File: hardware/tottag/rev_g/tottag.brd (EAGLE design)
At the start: 68.1 x 39.5 mm, 198 parts, among them J1 USB4110-GF-A, J2 DM3AT-SF-PEJM5, J3 TC2030-JLINK-NL-2SIDE, J4 TC2030-JLINK-NL-2SIDE, J5 MOLEX-PICO-SPOX-3SIDE, Q1 CSD75207W15, Q4 CSD75207W15, T1 HHM1595A1, U1 DW1000, U10 STM32F091CC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

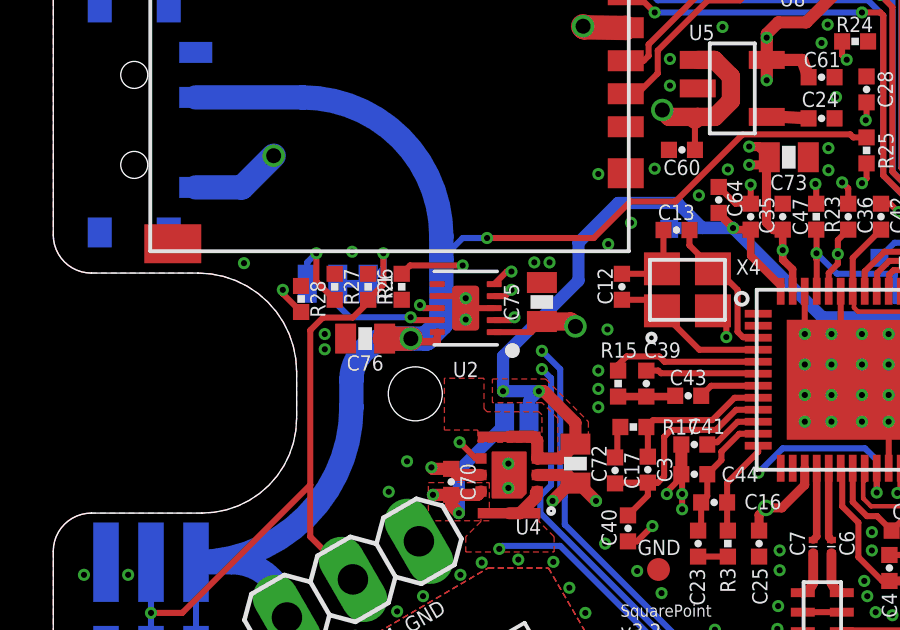
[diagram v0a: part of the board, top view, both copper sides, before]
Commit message: rev_g: design review fixes
 - Unify `!AD_EN` naming
 - C75/C76 10µF -> 1µF
 - Add battery pack details
 - Add NTC math details
 - Clarify switch on power diagram
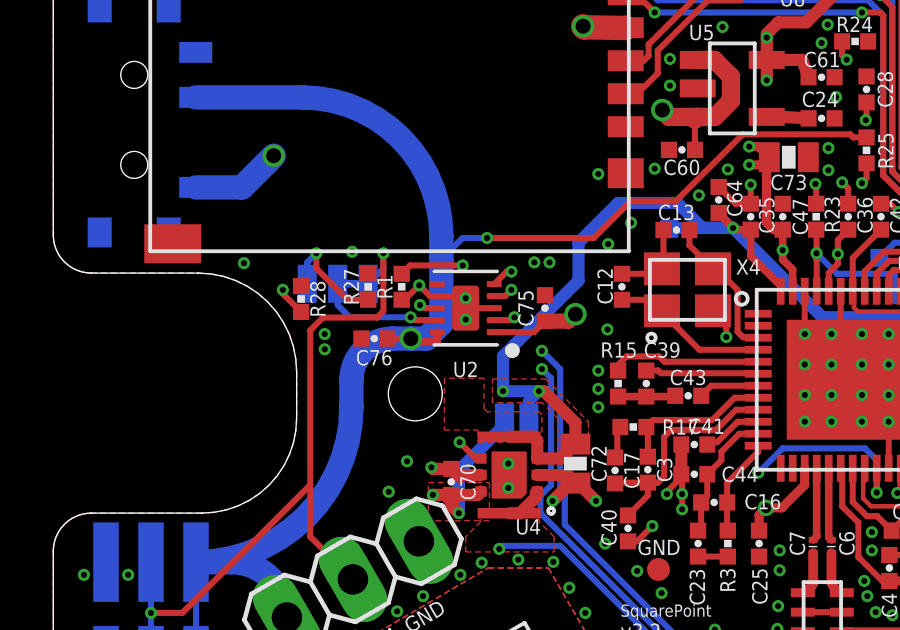
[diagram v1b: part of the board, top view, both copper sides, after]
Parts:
- removed R26: 249k, passives:0402_RES
- C75, C76: value 10uF -> 1uF; device passives:0603_CAP -> passives:0402_CAP
- moved R27 1.12 mm to (-23.6, 17.1)
- moved C76 0.30 mm to (-23.4, 15.3)
- moved C75 0.23 mm to (-17.7, 16.4)
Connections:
- net !AD-EN renamed !AD_EN
- net BATT_THERM: no longer R26.2
- net GND: no longer R26.1
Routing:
- net GND: track 148.3 -> 149.8 mm, vias 516 -> 517
- net N$47: track 2.95 -> 3.81 mm

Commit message: rev_g: correct thermistor prefix (R36 -> RT1)
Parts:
- renumbered R36 to RT1
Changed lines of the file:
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@@
 <attribute name="VALUE" x="1.7526" y="-4.3942" size="0.508" layer="27" font="vector" ratio="18" rot="R180" align="bottom-center"/>
 </element>
-<element name="R36" library="passives" library_urn="urn:adsk.eagle:library:20904581" package="0402_RES" package3d_urn="urn:adsk.eagle:package:20904668/2" value="10k@25C" x="0.9144" y="-3.0734" smashed="yes" rot="R270">
+<element name="RT1" library="passives" library_urn="urn:adsk.eagle:library:20904581" package="0402_RES" package3d_urn="urn:adsk.eagle:package:20904668/2" value="10k@25C" x="0.9144" y="-3.0734" smashed="yes" rot="R270">
 <attribute name="NAME" x="1.2954" y="-3.0734" size="0.508" layer="25" font="vector" ratio="18" rot="R270" align="bottom-center"/>
 <attribute name="VALUE" x="-0.4826" y="-3.0734" size="0.508" layer="27" font="vector" ratio="18" rot="R270" align="bottom-center"/>
@@
 <signal name="N$68">
 <contactref element="JP3" pad="3"/>
-<contactref element="R36" pad="2"/>
+<contactref element="RT1" pad="2"/>
 <wire x1="1.4224" y1="-3.4544" x2="1.4224" y2="-3.2512" width="0.2032" layer="16"/>
 <wire x1="1.4224" y1="-3.2512" x2="1.9304" y2="-2.7432" width="0.2032" layer="16"/>
@@
 </signal>
 <signal name="N$69">
-<contactref element="R36" pad="1"/>
+<contactref element="RT1" pad="1"/>
 <contactref element="R37" pad="2"/>
 <wire x1="0.9144" y1="-2.64033125" x2="0.9144" y2="-1.65226875" width="0.2032" layer="1"/>

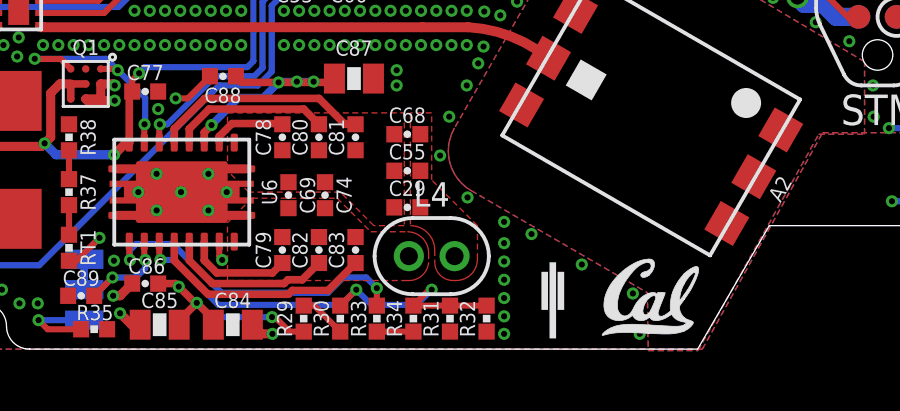
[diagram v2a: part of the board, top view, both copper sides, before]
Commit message: rev_g: Fix R31, R32 series / parallel
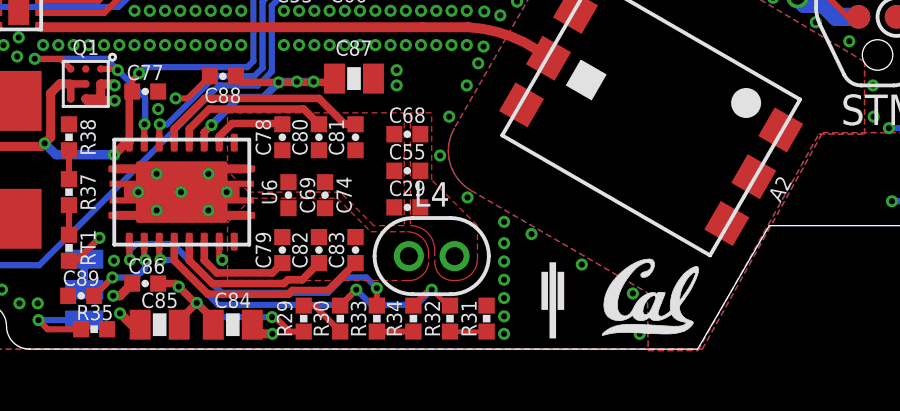
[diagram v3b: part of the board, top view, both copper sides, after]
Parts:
- moved R31 1.22 mm to (14.8, -5.44)
- moved R32 1.22 mm to (13.6, -5.44), turned to 270 degrees
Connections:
- new net N$28: R31.1, R32.2
- net BQ_FOD: now also R32.1; no longer R31.2, R32.2
- net GND: now also R31.2; no longer R31.1, R32.1
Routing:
- net BQ_FOD: track 14.9 -> 13.3 mm
- net N$28: track 0.00 -> 1.22 mm
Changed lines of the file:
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@@
 <attribute name="VALUE" x="11.3538" y="-5.4356" size="0.508" layer="27" font="vector" ratio="18" rot="R90" align="bottom-center"/>
 </element>
-<element name="R31" library="passives" library_urn="urn:adsk.eagle:library:20904581" package="0402_RES" package3d_urn="urn:adsk.eagle:package:20904668/2" value="97.6" x="13.6144" y="-5.4356" smashed="yes" rot="R90">
-<attribute name="DIGIKEY" value="RMCF0402FT97R6CT-ND" x="13.6144" y="-5.4356" size="1.778" layer="27" rot="R90" display="off"/>
-<attribute name="MPN" value="RMCF0402FT97R6" x="13.6144" y="-5.4356" size="1.778" layer="27" rot="R90" display="off"/>
-<attribute name="NAME" x="13.2334" y="-5.4356" size="0.508" layer="25" font="vector" ratio="18" rot="R90" align="bottom-center"/>
-<attribute name="VALUE" x="15.0114" y="-5.4356" size="0.508" layer="27" font="vector" ratio="18" rot="R90" align="bottom-center"/>
-</element>
-<element name="R32" library="passives" library_urn="urn:adsk.eagle:library:20904581" package="0402_RES" package3d_urn="urn:adsk.eagle:package:20904668/2" value="97.6" x="14.8336" y="-5.4356" smashed="yes" rot="R90">
+<element name="R31" library="passives" library_urn="urn:adsk.eagle:library:20904581" package="0402_RES" package3d_urn="urn:adsk.eagle:package:20904668/2" value="97.6" x="14.8336" y="-5.4356" smashed="yes" rot="R90">
 <attribute name="DIGIKEY" value="RMCF0402FT97R6CT-ND" x="14.8336" y="-5.4356" size="1.778" layer="27" rot="R90" display="off"/>
 <attribute name="MPN" value="RMCF0402FT97R6" x="14.8336" y="-5.4356" size="1.778" layer="27" rot="R90" display="off"/>
-<attribute name="NAME" x="14.4526" y="-5.4356" size="0.508" layer="25" font="vector" ratio="18" rot="R90" align="bottom-center"/>
+<attribute name="NAME" x="14.5034" y="-5.4356" size="0.508" layer="25" font="vector" ratio="18" rot="R90" align="bottom-center"/>
 <attribute name="VALUE" x="16.2306" y="-5.4356" size="0.508" layer="27" font="vector" ratio="18" rot="R90" align="bottom-center"/>
 </element>
+<element name="R32" library="passives" library_urn="urn:adsk.eagle:library:20904581" package="0402_RES" package3d_urn="urn:adsk.eagle:package:20904668/2" value="97.6" x="13.6144" y="-5.4356" smashed="yes" rot="R270">
+<attribute name="DIGIKEY" value="RMCF0402FT97R6CT-ND" x="13.6144" y="-5.4356" size="1.778" layer="27" rot="R270" display="off"/>
+<attribute name="MPN" value="RMCF0402FT97R6" x="13.6144" y="-5.4356" size="1.778" layer="27" rot="R270" display="off"/>
+<attribute name="NAME" x="13.2842" y="-5.4356" size="0.508" layer="25" font="vector" ratio="18" rot="R90" align="bottom-center"/>
+<attribute name="VALUE" x="12.2174" y="-5.4356" size="0.508" layer="27" font="vector" ratio="18" rot="R270" align="bottom-center"/>
+</element>
 <element name="R33" library="passives" library_urn="urn:adsk.eagle:library:20904581" package="0402_RES" package3d_urn="urn:adsk.eagle:package:20904668/2" value="162" x="11.176" y="-5.4356" smashed="yes" rot="R270">
 <attribute name="DIGIKEY" value="RMCF0402FT162RCT-ND" x="11.176" y="-5.4356" size="1.778" layer="27" rot="R270" display="off"/>
@@
 <contactref element="U6" pad="1"/>
 <contactref element="U6" pad="PAD"/>
-<contactref element="R31" pad="1"/>
-<contactref element="R32" pad="1"/>
 <via x="19.7104" y="-4.5974" extent="1-16" drill="0.2032"/>
 <via x="18.0086" y="-3.6322" extent="1-16" drill="0.2032"/>
@@
 <wire x1="-21.27" y1="16.7576" x2="-21.5074" y2="16.7576" width="0.2032" layer="1"/>
 <wire x1="-21.5074" y1="16.7576" x2="-21.8694" y2="17.1196" width="0.2032" layer="1"/>
+<contactref element="R31" pad="2"/>
 </signal>
 <signal name="VUSB">
@@
 </signal>
 <signal name="BQ_FOD">
-<contactref element="R31" pad="2"/>
-<contactref element="R32" pad="2"/>
 <contactref element="U6" pad="14"/>
 <contactref element="R30" pad="2"/>
 <contactref element="R34" pad="2"/>
-<wire x1="14.8336" y1="-5.00253125" x2="13.6144" y2="-5.00253125" width="0.2032" layer="1"/>
-<wire x1="13.6144" y1="-5.00253125" x2="12.3952" y2="-5.00253125" width="0.2032" layer="1"/>
 <wire x1="3.9236" y1="-2.8692" x2="3.9236" y2="-3.441" width="0.2032" layer="1"/>
 <wire x1="3.9236" y1="-3.441" x2="3.9624" y2="-3.4798" width="0.2032" layer="1"/>
@@
 <wire x1="12.4968" y1="-4.9784" x2="13.0048" y2="-4.4704" width="0.2032" layer="16"/>
 <wire x1="10.9982" y1="-4.9784" x2="12.4968" y2="-4.9784" width="0.2032" layer="16"/>
+<contactref element="R32" pad="1"/>
+<wire x1="13.6144" y1="-5.00253125" x2="13.53693125" y2="-5.00253125" width="0.1524" layer="1"/>
+<wire x1="13.53693125" y1="-5.00253125" x2="13.0048" y2="-4.4704" width="0.1524" layer="1"/>
 </signal>
 <signal name="BQ_RECT">
@@
 <via x="-18.8976" y="10.3632" extent="1-16" drill="0.2032"/>
 </signal>
+<signal name="N$28">
+<contactref element="R31" pad="1"/>
+<contactref element="R32" pad="2"/>
+<wire x1="14.8336" y1="-5.86866875" x2="13.6144" y2="-5.86866875" width="0.1524" layer="1"/>
+</signal>
 </signals>

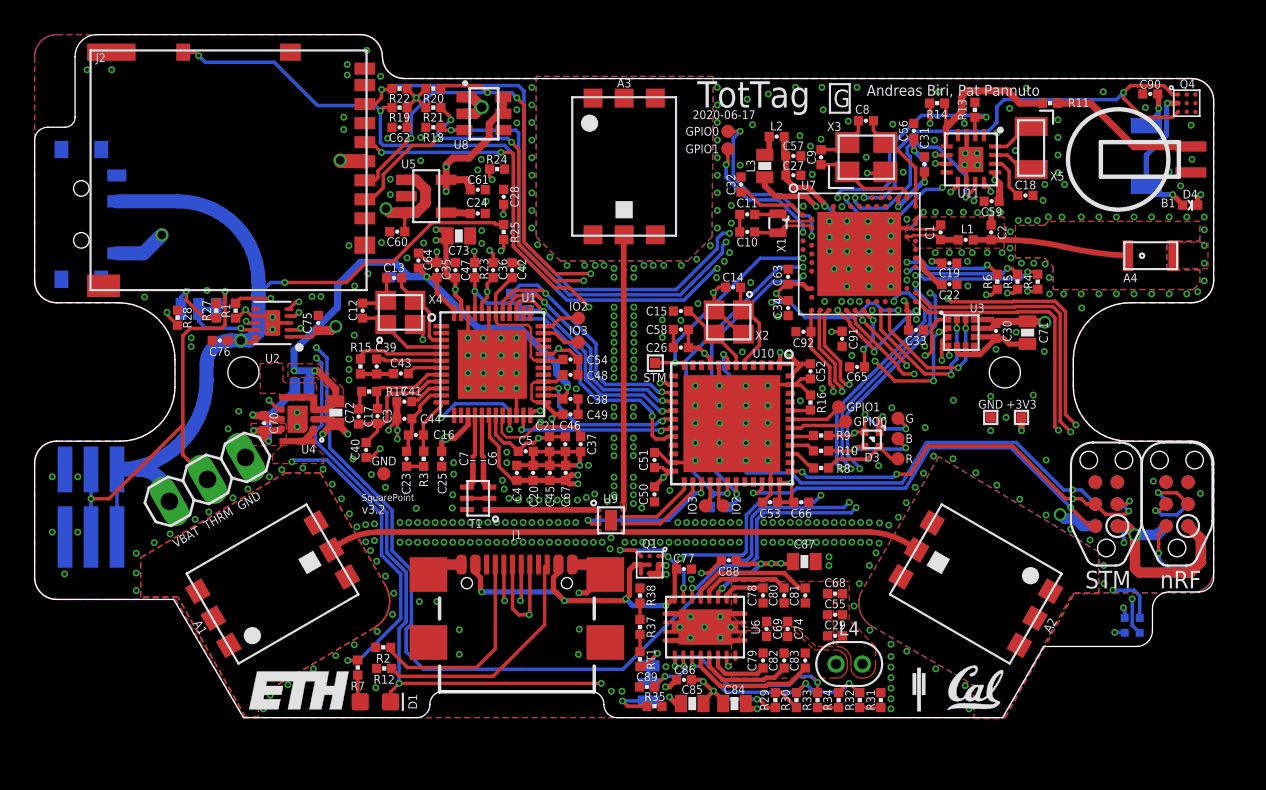
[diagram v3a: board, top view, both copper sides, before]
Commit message: rev_g: [WIP] design review fixes, board file
 - cleanup angle on BATT_THERM
 - C60 -> P1 not P3; connect GND
 - C61: route 3v3 to filter through; GND back to P2
 - More GND around U6 IC
 - P1/P2 GND pours for U6
 - Re-route VQI out of U6 to go expressly through filter caps before plane
 - Improve filtering routing of RECT signal
 - Rotate R29 to clean up routing a bit
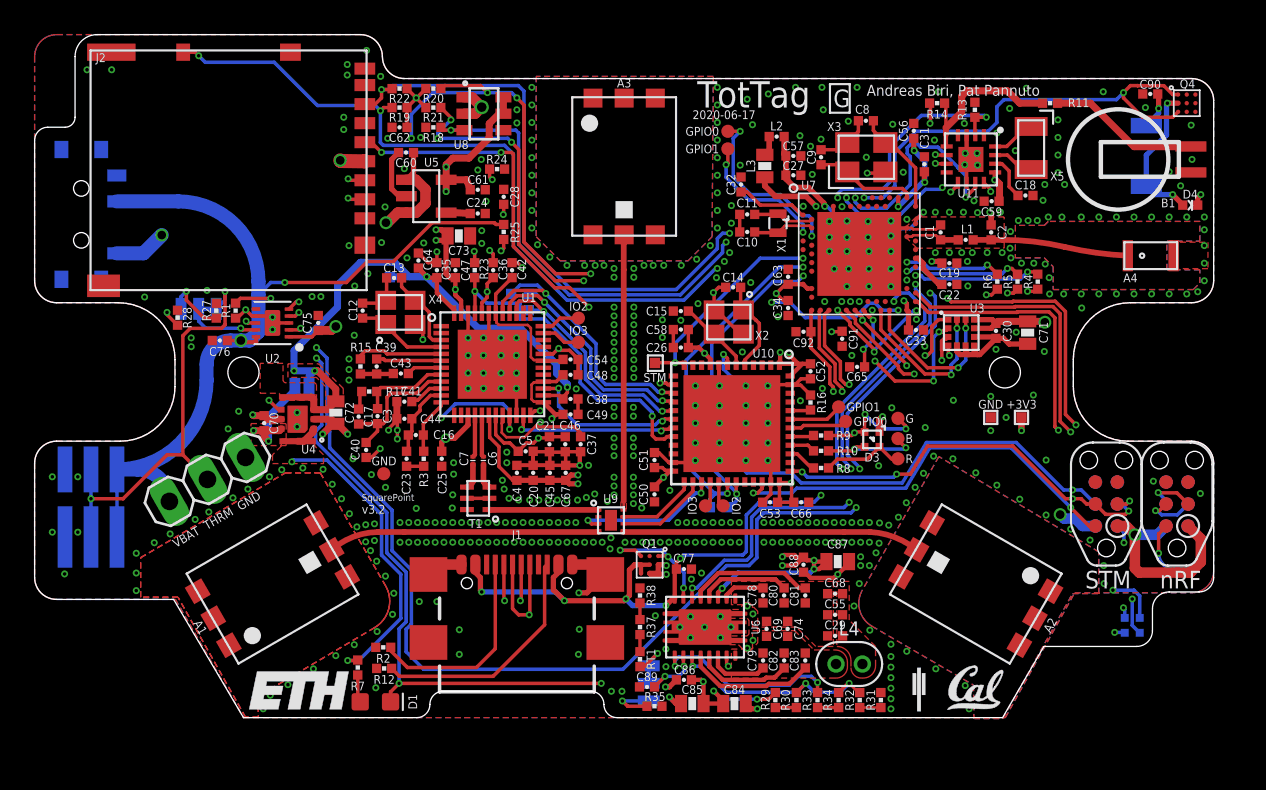
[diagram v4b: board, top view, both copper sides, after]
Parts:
- moved C60 4.60 mm to (-12.6, 26.2)
- moved C88 4.33 mm to (10.4, 2.39), turned to 270 degrees
- moved C87 1.93 mm to (12.3, 2.57)
- turned R29 to 270 degrees
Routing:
- net VQI: track 13.5 -> 17.5 mm, vias 7 -> 8
- net GND: track 149.8 -> 153.5 mm, vias 517 -> 523
- net NRF_MOSI: track 66.3 -> 68.1 mm, vias 10 -> 11
- net !NRF_CS_SD: track 42.7 -> 44.2 mm, vias 6 -> 7
- net BATT_THERM: track 25.7 -> 25.0 mm

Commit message: rev_g: [WIP] design review fixes
 - Replace battery pinheader with individual pieces (allows U4 move later)
 - Fix lost ground plane (?!)
 - Then isolate and stitch up wireless ground plane to primary ground plane
 - Move routing from layer 2 to 15 where trivial to do so
 - Clean up C15 / C26 / C58 caps
 - Separate SD card passives from DW cap bank
 - Align R28
 - Add more vias around 3v3 / 1v8 conversion
 - Move U4 regulator farther from DW; add line of shield vias
 - Several plane cleanups with old route-arounds removed
 - Clean up some silk overlap errors
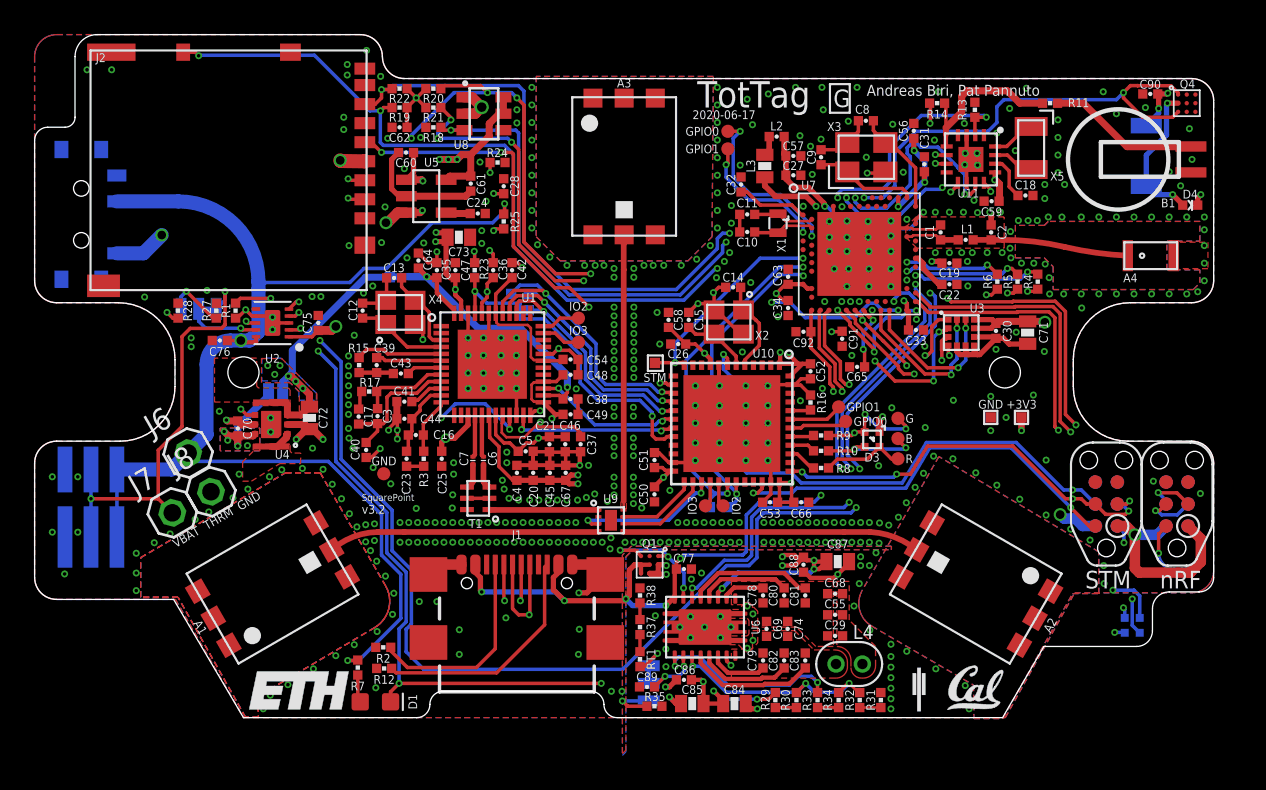
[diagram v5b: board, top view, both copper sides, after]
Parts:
- added J7, J8: (no value), pinhead:1X01
- J6: device pinhead:1X03 -> pinhead:1X01
- moved J6 1.89 mm to (-25.2, 8.84)
- moved U4 1.55 mm to (-20.4, 10.5)
- moved C70 1.55 mm to (-22.3, 10.3)
- moved C72 1.55 mm to (-18.2, 10.9)
- moved JP1 1.55 mm to (-20.1, 12.2)
- moved C58 0.90 mm to (2.57, 16.5), turned to 90 degrees
- moved C15 0.68 mm to (3.73, 16.5), turned to 90 degrees
- moved C28 0.61 mm to (-6.96, 24.3)
- moved R25 0.61 mm to (-6.96, 22.2)
- moved C61 0.54 mm to (-8.86, 24.4), turned to 270 degrees
- moved R28 0.41 mm to (-25.8, 17.1)
- moved R24 0.38 mm to (-7.32, 25.6)
- moved C26 0.25 mm to (3.12, 15.1)
- moved R15 0.11 mm to (-15.3, 13.9)
- moved C39 0.08 mm to (-14.3, 13.9)
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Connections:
- net BATT_THERM: now also J7.1; no longer J6.2
- net GND: now also J8.1; no longer J6.3
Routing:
- net +3V3: track 159.0 -> 146.6 mm, vias 34 -> 39
- net GND: track 153.5 -> 158.5 mm, vias 523 -> 529
- net +1V8: track 40.7 -> 37.5 mm, vias 4 -> 8
- net VBAT: track 76.3 -> 73.7 mm, vias 4 -> 3
- net REG_EN: track 17.7 -> 18.8 mm
- net !CHG: track 76.6 -> 76.0 mm
- net !DW_RST: track 9.15 -> 8.55 mm
- net VBAT_SWITCHED: track 22.9 -> 23.1 mm, vias 2 -> 4
- added copper zone on layer 16, net +1V8
- added copper zone on layer 16, net +3V3
- added copper zone on layer 15, net GND
- removed copper zone on layer 1, net N$36
- removed copper zone on layer 16, net N$36
